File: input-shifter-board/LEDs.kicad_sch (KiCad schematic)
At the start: 96 parts

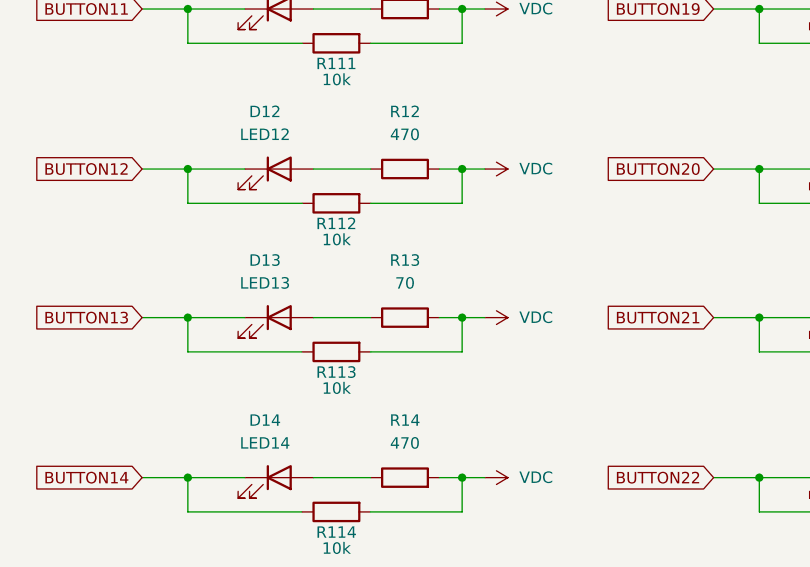
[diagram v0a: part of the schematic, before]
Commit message: add part numbers for all components, rename sheet with active parts
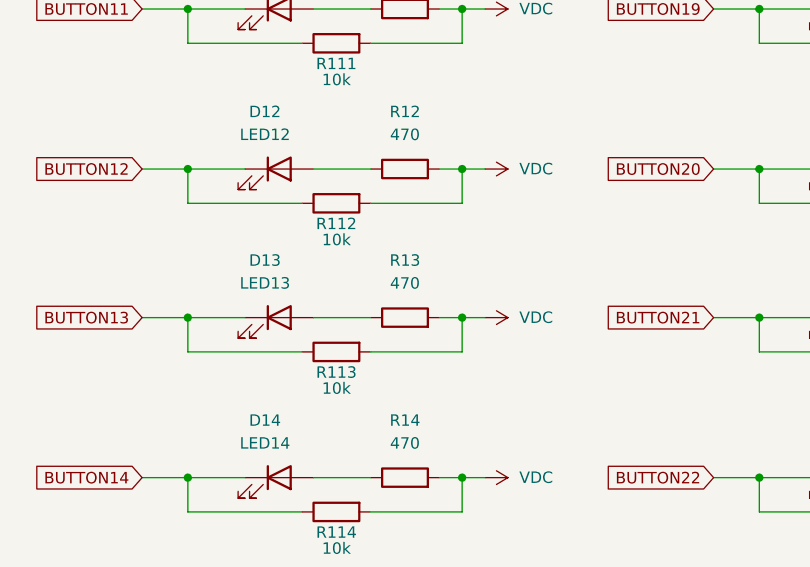
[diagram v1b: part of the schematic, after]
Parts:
- D1, D10, D11, D12, D13, D14, D15, D16, D17, D18, D19, D2, D20, D21, D22, D23, D24, D25, D26, D27, D28, D29, D3, D30, D31, D32, D4, D5, D6, D7, D8, D9: LCSC (none) -> C130722
- R1, R10, R11, R12, R14, R15, R16, R17, R18, R19, R2, R20, R21, R22, R23, R24, R25, R26, R27, R28, R29, R3, R30, R31, R32, R4, R5, R6, R7, R8, R9: LCSC (none) -> C25117
- R101, R102, R103, R104, R105, R106, R107, R108, R109, R110, R111, R112, R113, R114, R115, R116, R117, R118, R119, R120, R121, R122, R123, R124, R125, R126, R127, R128, R129, R130, R131, R132: LCSC (none) -> C25744
- R13: value 70 -> 470; LCSC (none) -> C25117
